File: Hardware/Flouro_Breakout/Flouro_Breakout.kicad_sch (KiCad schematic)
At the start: 0 parts

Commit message: Added in headers
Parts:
- added J? (x2): Conn_02x20_Odd_Even_MountingPin, symbol Connector_Generic_MountingPin:Conn_02x20_Odd_Even_MountingPin
- added U?: NUCLEO64-F411RE, Module:ST_Morpho_Connector_144_STLink, symbol MCU_Module:NUCLEO64-F411RE

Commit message: Adding more bits
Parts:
- added Conn? (x2): AndersonPP, MRDT_Connectors:Square_Anderson_2_H_Side_By_Side, symbol MRDT_Connectors:AndersonPP
- added Conn?: Molex_SL_06, Connector_Molex:Molex_SL_171971-0006_1x06_P2.54mm_Vertical, symbol Molex_SL_06:Molex_SL_06
- added Q?: Q_PNP_ECB, symbol Device:Q_PNP_ECB
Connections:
- new net +12V: Conn?.2 (V+Log)
- new net +3V3: Conn?.1
- new net CCD_ICG: Conn?.5
- new net CCD_MC: Conn?.3
- new net CCD_OS: Conn?.6
- new net CCD_SH: Conn?.4
- new net GND: Conn?.1 (GND), Conn?.2
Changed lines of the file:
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@@
     (company "MRDT")
   )
+  (wire (pts (xy 199.39 56.515) (xy 209.55 56.515))
+    (stroke (width 0) (type default) (color 0 0 0 0))
+  )
+  (wire (pts (xy 229.235 116.205) (xy 222.885 116.205))
+    (stroke (width 0) (type default) (color 0 0 0 0))
+  )
+  (wire (pts (xy 198.12 64.135) (xy 209.55 64.135))
+    (stroke (width 0) (type default) (color 0 0 0 0))
+  )
+  (wire (pts (xy 198.12 59.055) (xy 209.55 59.055))
+    (stroke (width 0) (type default) (color 0 0 0 0))
+  )
+  (wire (pts (xy 198.12 66.675) (xy 209.55 66.675))
+    (stroke (width 0) (type default) (color 0 0 0 0))
+  )
+  (wire (pts (xy 199.39 52.07) (xy 199.39 56.515))
+    (stroke (width 0) (type default) (color 0 0 0 0))
+  )
+  (wire (pts (xy 203.2 53.975) (xy 209.55 53.975))
+    (stroke (width 0) (type default) (color 0 0 0 0))
+  )
+  (wire (pts (xy 209.55 61.595) (xy 198.12 61.595))
+    (stroke (width 0) (type default) (color 0 0 0 0))
+  )
+  (wire (pts (xy 195.58 52.07) (xy 199.39 52.07))
+    (stroke (width 0) (type default) (color 0 0 0 0))
+  )
+  (wire (pts (xy 195.58 114.3) (xy 201.93 114.3))
+    (stroke (width 0) (type default) (color 0 0 0 0))
+  )
   (image (at 13.97 196.85) (scale 0.00627523)
     (data
@@
     )
   )
+  (global_label "CCD_OS" (shape output) (at 198.12 66.675 180) (fields_autoplaced)
+    (effects (font (size 1 1)) (justify right))
+    (property "Intersheet References" "${INTERSHEET_REFS}" (id 0) (at 190.5281 66.6125 0)
+      (effects (font (size 1 1)) (justify right) hide)
+    )
+  )
+  (global_label "CCD_SH" (shape input) (at 198.12 61.595 180) (fields_autoplaced)
+    (effects (font (size 1 1)) (justify right))
+    (property "Intersheet References" "${INTERSHEET_REFS}" (id 0) (at 190.5281 61.5325 0)
+      (effects (font (size 1 1)) (justify right) hide)
+    )
+  )
+  (global_label "CCD_ICG" (shape input) (at 198.12 64.135 180) (fields_autoplaced)
+    (effects (font (size 1 1)) (justify right))
+    (property "Intersheet References" "${INTERSHEET_REFS}" (id 0) (at 190.0519 64.0725 0)
+      (effects (font (size 1 1)) (justify right) hide)
+    )
+  )
+  (global_label "CCD_MC" (shape input) (at 198.12 59.055 180) (fields_autoplaced)
+    (effects (font (size 1 1)) (justify right))
+    (property "Intersheet References" "${INTERSHEET_REFS}" (id 0) (at 190.3852 58.9925 0)
+      (effects (font (size 1 1)) (justify right) hide)
+    )
+  )
+  (symbol (lib_id "MRDT_Connectors:AndersonPP") (at 185.42 116.84 0) (unit 1)
+    (in_bom yes) (on_board yes)
+    (property "Reference" "Conn?" (id 0) (at 190.7032 107.0102 0)
+      (effects (font (size 1.524 1.524)))
+    )
+    (property "Value" "AndersonPP" (id 1) (at 190.7032 109.7026 0)
+      (effects (font (size 1.524 1.524)))
+    )
+    (property "Footprint" "MRDT_Connectors:Square_Anderson_2_H_Side_By_Side" (id 2) (at 181.61 130.81 0)
+      (effects (font (size 1.524 1.524)) hide)
+    )
+    (property "Datasheet" "" (id 3) (at 181.61 130.81 0)
+      (effects (font (size 1.524 1.524)) hide)
+    )
+    (pin "1")
+    (pin "2")
+    (pin "3")
+    (pin "4")
+    (pin "1")
+  )
+  (symbol (lib_id "Device:Q_PNP_ECB") (at 199.39 78.74 0) (unit 1)
+    (in_bom yes) (on_board yes) (fields_autoplaced)
+    (property "Reference" "Q?" (id 0) (at 204.47 77.4699 0)
+      (effects (font (size 1.27 1.27)) (justify left))
+    )
+    (property "Value" "Q_PNP_ECB" (id 1) (at 204.47 80.0099 0)
+      (effects (font (size 1.27 1.27)) (justify left))
+    )
+    (property "Footprint" "" (id 2) (at 204.47 76.2 0)
+      (effects (font (size 1.27 1.27)) hide)
+    )
+    (property "Datasheet" "~" (id 3) (at 199.39 78.74 0)
+      (effects (font (size 1.27 1.27)) hide)
+    )
+    (pin "1")
+    (pin "2")
+    (pin "3")
+  )
+  (symbol (lib_id "MRDT_Connectors:AndersonPP") (at 212.725 118.745 0) (unit 2)
+    (in_bom yes) (on_board yes) (fields_autoplaced)
+    (property "Reference" "Conn?" (id 0) (at 215.265 108.585 0)
+      (effects (font (size 1.524 1.524)))
+    )
+    (property "Value" "AndersonPP" (id 1) (at 215.265 112.395 0)
+      (effects (font (size 1.524 1.524)))
+    )
+    (property "Footprint" "MRDT_Connectors:Square_Anderson_2_H_Side_By_Side" (id 2) (at 208.915 132.715 0)
+      (effects (font (size 1.524 1.524)) hide)
+    )
+    (property "Datasheet" "" (id 3) (at 208.915 132.715 0)
+      (effects (font (size 1.524 1.524)) hide)
+    )
+    (pin "1")
+    (pin "2")
+    (pin "3")
+    (pin "4")
+    (pin "1")
+  )
+  (symbol (lib_id "power:GND") (at 201.93 114.3 0) (unit 1)
+    (in_bom yes) (on_board yes)
+    (property "Reference" "#PWR?" (id 0) (at 201.93 120.65 0)
+      (effects (font (size 1.27 1.27)) hide)
+    )
+    (property "Value" "GND" (id 1) (at 202.057 118.6942 0))
+    (property "Footprint" "" (id 2) (at 201.93 114.3 0)
+      (effects (font (size 1.27 1.27)) hide)
+    )
+    (property "Datasheet" "" (id 3) (at 201.93 114.3 0)
+      (effects (font (size 1.27 1.27)) hide)
+    )
+    (pin "1")
+  )
+  (symbol (lib_id "power:GND") (at 195.58 52.07 0) (unit 1)
+    (in_bom yes) (on_board yes) (fields_autoplaced)
+    (property "Reference" "#PWR?" (id 0) (at 195.58 58.42 0)
+      (effects (font (size 1.27 1.27)) hide)
+    )
+    (property "Value" "GND" (id 1) (at 195.58 56.5134 0))
+    (property "Footprint" "" (id 2) (at 195.58 52.07 0)
+      (effects (font (size 1.27 1.27)) hide)
+    )
+    (property "Datasheet" "" (id 3) (at 195.58 52.07 0)
+      (effects (font (size 1.27 1.27)) hide)
+    )
+    (pin "1")
+  )
   (symbol (lib_id "Connector_Generic_MountingPin:Conn_02x20_Odd_Even_MountingPin") (at 143.51 81.28 0) (unit 1)
     (in_bom yes) (on_board yes) (fields_autoplaced)
@@
     (pin "MP")
   )
+  (symbol (lib_id "Molex_SL_06:Molex_SL_06") (at 214.63 65.405 0) (unit 1)
+    (in_bom yes) (on_board yes) (fields_autoplaced)
+    (property "Reference" "Conn?" (id 0) (at 217.805 59.3488 0)
+      (effects (font (size 1.524 1.524)) (justify left))
+    )
+    (property "Value" "Molex_SL_06" (id 1) (at 217.805 62.3422 0)
+      (effects (font (size 1.524 1.524)) (justify left))
+    )
+    (property "Footprint" "Connector_Molex:Molex_SL_171971-0006_1x06_P2.54mm_Vertical" (id 2) (at 214.63 65.405 0)
+      (effects (font (size 1.524 1.524)) hide)
+    )
+    (property "Datasheet" "" (id 3) (at 214.63 65.405 0)
+      (effects (font (size 1.524 1.524)) hide)
+    )
+    (pin "1")
+    (pin "2")
+    (pin "3")
+    (pin "4")
+    (pin "5")
+    (pin "6")
+  )
+  (symbol (lib_id "power:+3V3") (at 203.2 53.975 0) (unit 1)
+    (in_bom yes) (on_board yes) (fields_autoplaced)
+    (property "Reference" "#PWR?" (id 0) (at 203.2 57.785 0)
+      (effects (font (size 1.27 1.27)) hide)
+    )
+    (property "Value" "+3V3" (id 1) (at 203.2 50.3992 0))
+    (property "Footprint" "" (id 2) (at 203.2 53.975 0)
+      (effects (font (size 1.27 1.27)) hide)
+    )
+    (property "Datasheet" "" (id 3) (at 203.2 53.975 0)
+      (effects (font (size 1.27 1.27)) hide)
+    )
+    (pin "1")
+  )
   (symbol (lib_id "Connector_Generic_MountingPin:Conn_02x20_Odd_Even_MountingPin") (at 171.45 81.28 0) (unit 1)
     (in_bom yes) (on_board yes) (fields_autoplaced)
@@
     (pin "MP")
   )
+  (symbol (lib_id "power:+12V") (at 229.235 116.205 0) (unit 1)
+    (in_bom yes) (on_board yes)
+    (property "Reference" "#PWR?" (id 0) (at 229.235 120.015 0)
+      (effects (font (size 1.27 1.27)) hide)
+    )
+    (property "Value" "+12V" (id 1) (at 229.616 111.8108 0))
+    (property "Footprint" "" (id 2) (at 229.235 116.205 0)
+      (effects (font (size 1.27 1.27)) hide)
+    )
+    (property "Datasheet" "" (id 3) (at 229.235 116.205 0)
+      (effects (font (size 1.27 1.27)) hide)
+    )
+    (pin "1")
+  )
   (symbol (lib_id "MCU_Module:NUCLEO64-F411RE") (at 80.01 97.79 0) (unit 1)
     (in_bom yes) (on_board yes) (fields_autoplaced)
@@
   )
   (symbol_instances
+    (path "/61b1071c-334c-4fa4-9c46-68e18b27bfb9"
+      (reference "#PWR?") (unit 1) (value "GND") (footprint "")
+    )
+    (path "/79f190bf-ce72-4aa6-b49d-0c6e691ffacb"
+      (reference "#PWR?") (unit 1) (value "GND") (footprint "")
+    )
+    (path "/d7aa172c-6e2e-43d1-aa12-3b36ed07d556"
+      (reference "#PWR?") (unit 1) (value "+3V3") (footprint "")
+    )
+    (path "/f50aeea7-667c-4c76-9470-f631ed8169e4"
+      (reference "#PWR?") (unit 1) (value "+12V") (footprint "")
+    )
+    (path "/0b2f7f62-7a46-4761-a435-9392bcea5d54"
+      (reference "Conn?") (unit 1) (value "AndersonPP") (footprint "MRDT_Connectors:Square_Anderson_2_H_Side_By_Side")
+    )
+    (path "/89c4caa7-fc66-46eb-acc0-1bed22f4bf13"
+      (reference "Conn?") (unit 1) (value "Molex_SL_06") (footprint "Connector_Molex:Molex_SL_171971-0006_1x06_P2.54mm_Vertical")
+    )
+    (path "/41efe818-6e23-400a-9bdc-b5cb71bb668d"
+      (reference "Conn?") (unit 2) (value "AndersonPP") (footprint "MRDT_Connectors:Square_Anderson_2_H_Side_By_Side")
+    )
     (path "/7f579713-2631-4946-9910-f20776f8de45"
       (reference "J?") (unit 1) (value "Conn_02x20_Odd_Even_MountingPin") (footprint "")
@@
       (reference "J?") (unit 1) (value "Conn_02x20_Odd_Even_MountingPin") (footprint "")
     )
+    (path "/0ea547f8-f0a6-4c4a-8038-cd1bf03400a4"
+      (reference "Q?") (unit 1) (value "Q_PNP_ECB") (footprint "")
+    )
     (path "/fcf20241-bee4-4a3a-87d1-81ed36df8642"

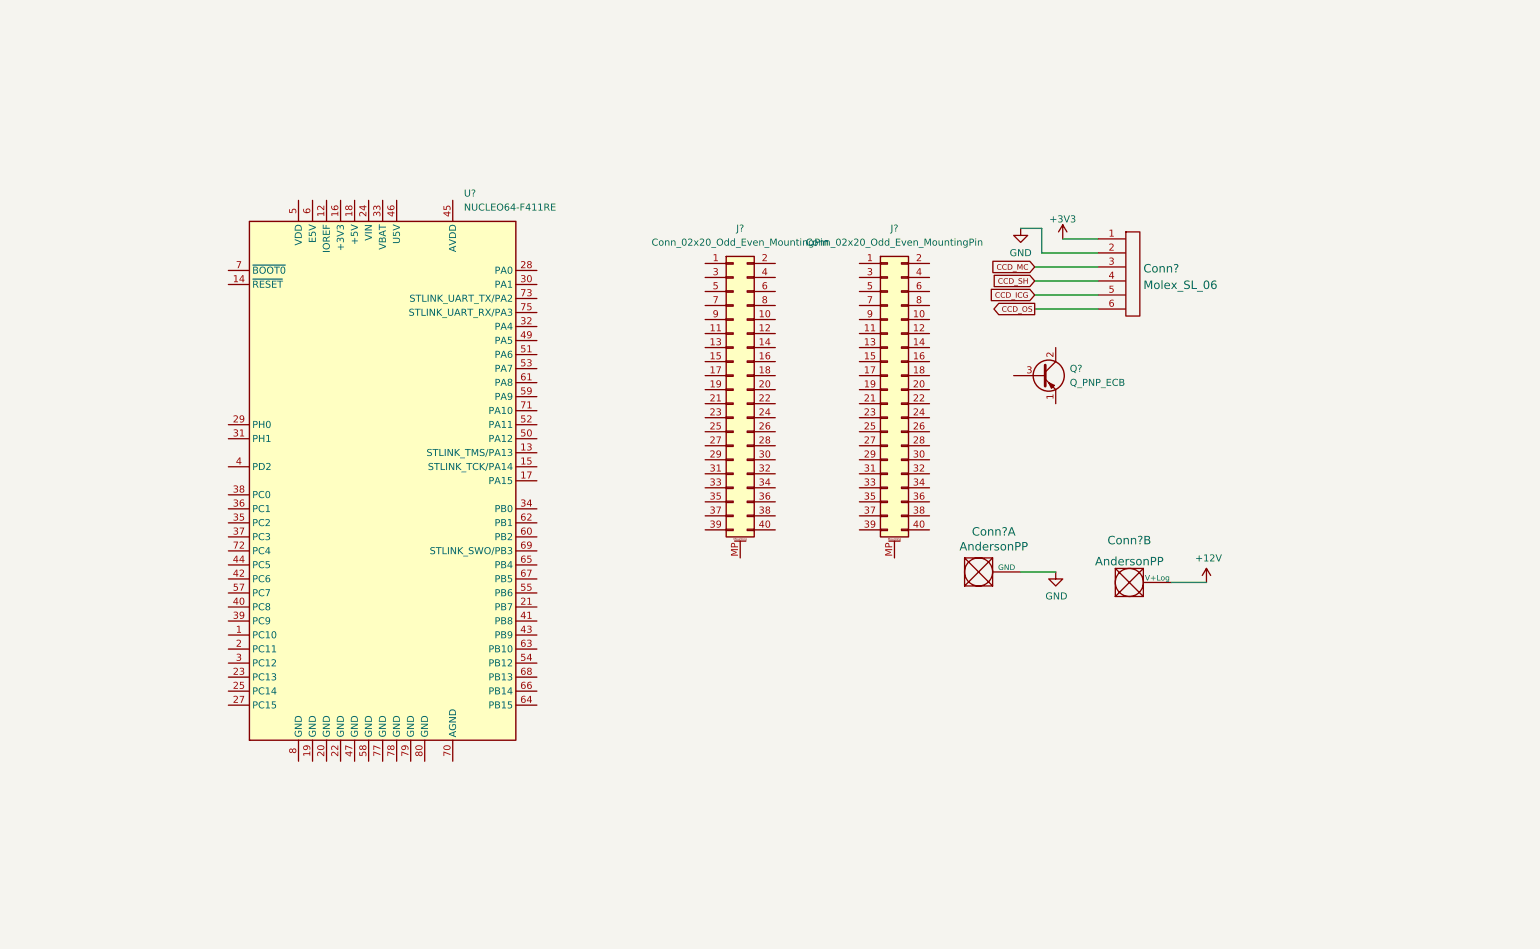
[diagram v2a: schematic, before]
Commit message: Added teensy and ethernet
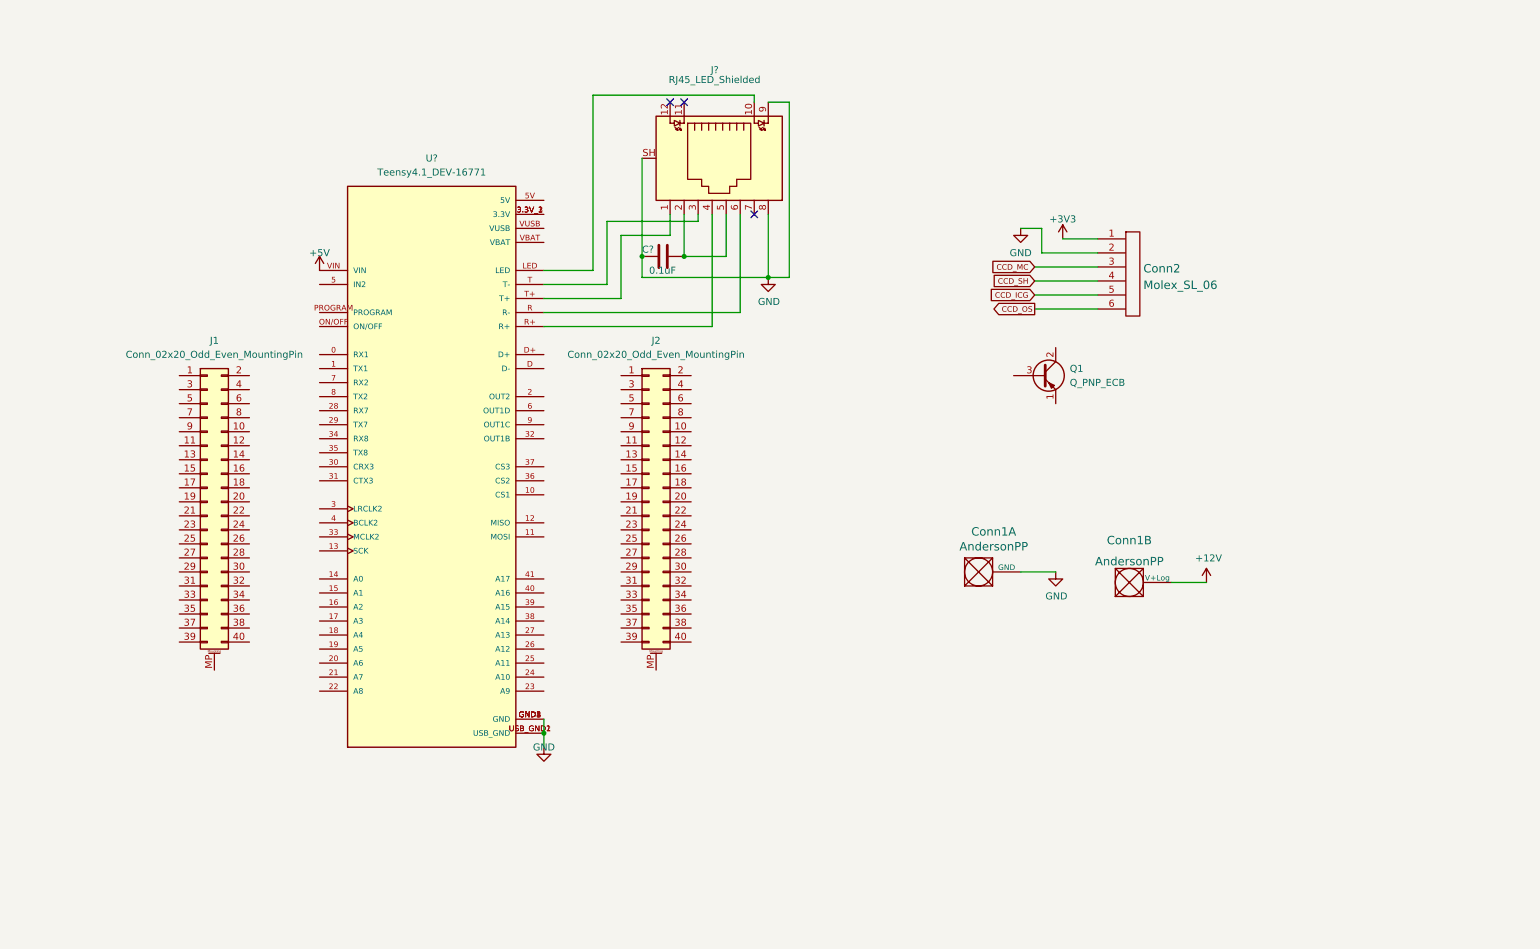
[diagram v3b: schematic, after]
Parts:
- removed U?: NUCLEO64-F411RE, Module:ST_Morpho_Connector_144_STLink, symbol MCU_Module:NUCLEO64-F411RE
- added C?: 0.1uF, Capacitor_SMD:C_0603_1608Metric_Pad1.08x0.95mm_HandSolder, symbol Device:C
- added J?: RJ45_LED_Shielded, MRDT_Connectors:RJ45_Teensy, symbol Connector:RJ45_LED_Shielded
- added U?: Teensy4.1_DEV-16771, MODULE_DEV-16771, symbol MRDT_Shields:Teensy4.1_DEV-16771
- gave numbers to parts that had none: 5
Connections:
- net GND: now also C?.2, J?.8, J?.9, J?.SH, U?.GND1 (GND), U?.GND2 (GND), U?.GND3 (GND), U?.GND4 (GND), U?.GND5 (GND), U?.USB_GND1 (USB_GND), U?.USB_GND2 (USB_GND)
- new net: J?.1, U?.T+
- new net: J?.10, U?.LED
- new net: C?.1, J?.2, J?.5
- new net: J?.3, U?.T (T-)
- new net: J?.4, U?.R+
- new net: J?.6, U?.R (R-)
- new net: U?.3.3V_1 (3.3V), U?.3.3V_2 (3.3V), U?.3.3V_3 (3.3V)
- new net +5V: U?.VIN
- no-connect marks 0 -> 3
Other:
- moved on the sheet: J1, J2

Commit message: Made CCD board and LED Rev2 folders
Starting schematic of CCD board.
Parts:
- removed Q1: Q_PNP_ECB, symbol Device:Q_PNP_ECB
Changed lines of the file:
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@@
     (pin "1")
-  )
-  (symbol (lib_id "Device:Q_PNP_ECB") (at 199.39 78.74 0) (unit 1)
-    (in_bom yes) (on_board yes) (fields_autoplaced)
-    (property "Reference" "Q1" (id 0) (at 204.47 77.4699 0)
-      (effects (font (size 1.27 1.27)) (justify left))
-    )
-    (property "Value" "Q_PNP_ECB" (id 1) (at 204.47 80.0099 0)
-      (effects (font (size 1.27 1.27)) (justify left))
-    )
-    (property "Footprint" "" (id 2) (at 204.47 76.2 0)
-      (effects (font (size 1.27 1.27)) hide)
-    )
-    (property "Datasheet" "~" (id 3) (at 199.39 78.74 0)
-      (effects (font (size 1.27 1.27)) hide)
-    )
-    (pin "1")
-    (pin "2")
-    (pin "3")
   )
   (symbol (lib_id "Connector:RJ45_LED_Shielded") (at 139.7 39.37 270) (unit 1)
@@
       (reference "J?") (unit 1) (value "RJ45_LED_Shielded") (footprint "MRDT_Connectors:RJ45_Teensy")
     )
-    (path "/0ea547f8-f0a6-4c4a-8038-cd1bf03400a4"
-      (reference "Q1") (unit 1) (value "Q_PNP_ECB") (footprint "")
-    )
     (path "/da2cf279-a4c5-471d-b9ff-93e148ea969a"
